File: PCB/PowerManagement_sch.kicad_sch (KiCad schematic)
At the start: 20 parts, among them CN1 S2B-PH-SM4-TB(LF)(SN), U1 BQ24074RGTR, U2 SGM2050XTRL20G/TR

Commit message: Finished schematic
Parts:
- C1: value 4.7uF 6.3V -> 4.7uF 10V
- C2: value 4.7uF -> 4.7uF 10V
- C3: value 1uF 6.3V -> 1uF 10V
- C4: value 10uF -> 10uF 10V
- C5: value 10uF -> 10uF 6.3V
- C6: value 100n -> 100nF 10V
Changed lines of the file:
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@@
 		(dnp no)
 		(property "Reference" "C5"
-			(at 243.078 66.802 90)
+			(at 243.078 71.882 90)
 			(effects
 				(font
@@
 			)
 		)
-		(property "Value" "10uF"
-			(at 235.204 67.056 90)
+		(property "Value" "10uF 6.3V"
+			(at 236.22 66.548 90)
 			(effects
 				(font
@@
 		(dnp no)
 		(property "Reference" "C6"
-			(at 258.064 101.6 90)
+			(at 252.73 101.6 90)
 			(effects
 				(font
@@
 			)
 		)
-		(property "Value" "100n"
-			(at 250.19 101.092 90)
+		(property "Value" "100nF 10V"
+			(at 250.952 106.172 90)
 			(effects
 				(font
@@
 			)
 		)
-		(property "Value" "1uF 6.3V"
+		(property "Value" "1uF 10V"
 			(at 112.268 153.924 0)
 			(effects
@@
 		(dnp no)
 		(property "Reference" "C4"
-			(at 258.064 96.52 90)
+			(at 252.222 96.52 90)
 			(effects
 				(font
@@
 			)
 		)
-		(property "Value" "10uF"
-			(at 250.19 96.012 90)
+		(property "Value" "10uF 10V"
+			(at 258.064 96.774 90)
 			(effects
 				(font
@@
 			)
 		)
-		(property "Value" "4.7uF 6.3V"
+		(property "Value" "4.7uF 10V"
 			(at 107.95 101.854 0)
 			(effects
@@
 			)
 		)
-		(property "Value" "4.7uF"
+		(property "Value" "4.7uF 10V"
 			(at 148.336 108.204 0)
 			(effects

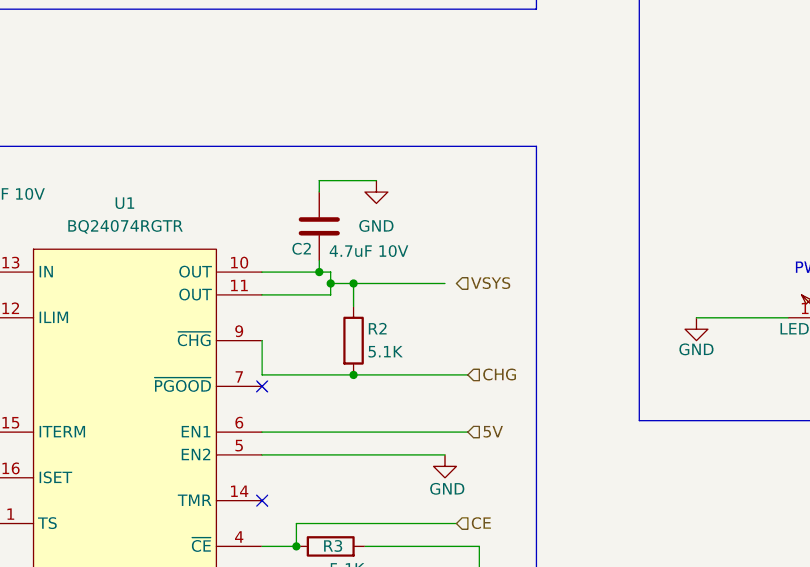
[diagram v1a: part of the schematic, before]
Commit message: pcb wired
- bldc driver + ldo left
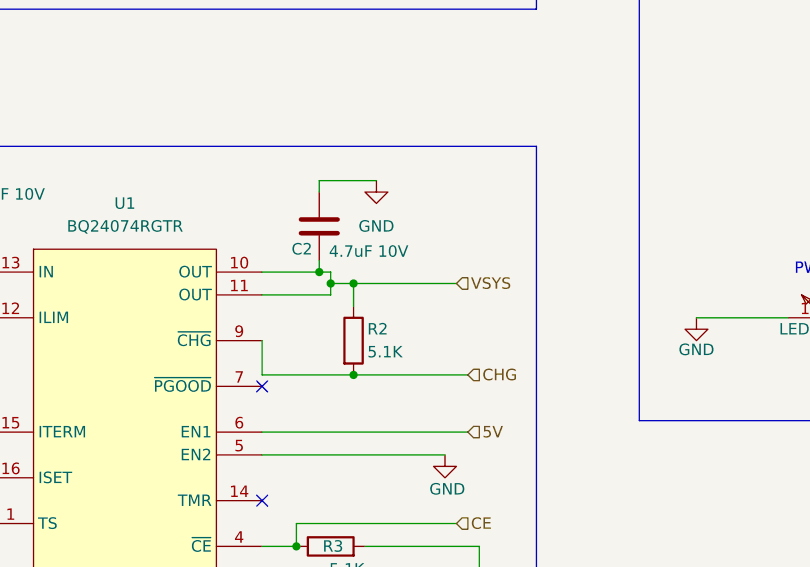
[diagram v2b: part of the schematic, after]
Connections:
- net VSYS: now also C2.1, R2.1, U1.10 (OUT), U1.11 (OUT)
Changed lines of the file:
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@@
 	(wire
 		(pts
-			(xy 142.24 111.76) (xy 152.4 111.76)
+			(xy 142.24 111.76) (xy 153.67 111.76)
 		)
 		(stroke

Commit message: PCB layout done
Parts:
- R1: value 2.2K -> 10K
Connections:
- no-connect marks 10 -> 13
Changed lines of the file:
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@@
 	)
 	(no_connect
+		(at 242.57 104.14)
+	)
+	(no_connect
 		(at 46.99 55.88)
 	)
@@
 	)
 	(no_connect
+		(at 217.17 91.44)
+	)
+	(no_connect
 		(at 46.99 40.64)
 	)
@@
 		(at 132.08 135.89)
 	)
+	(no_connect
+		(at 217.17 88.9)
+	)
 	(wire
 		(pts
@@
 			)
 		)
-		(property "Value" "2.2K"
+		(property "Value" "10K"
 			(at 208.28 115.57 90)
 			(effects

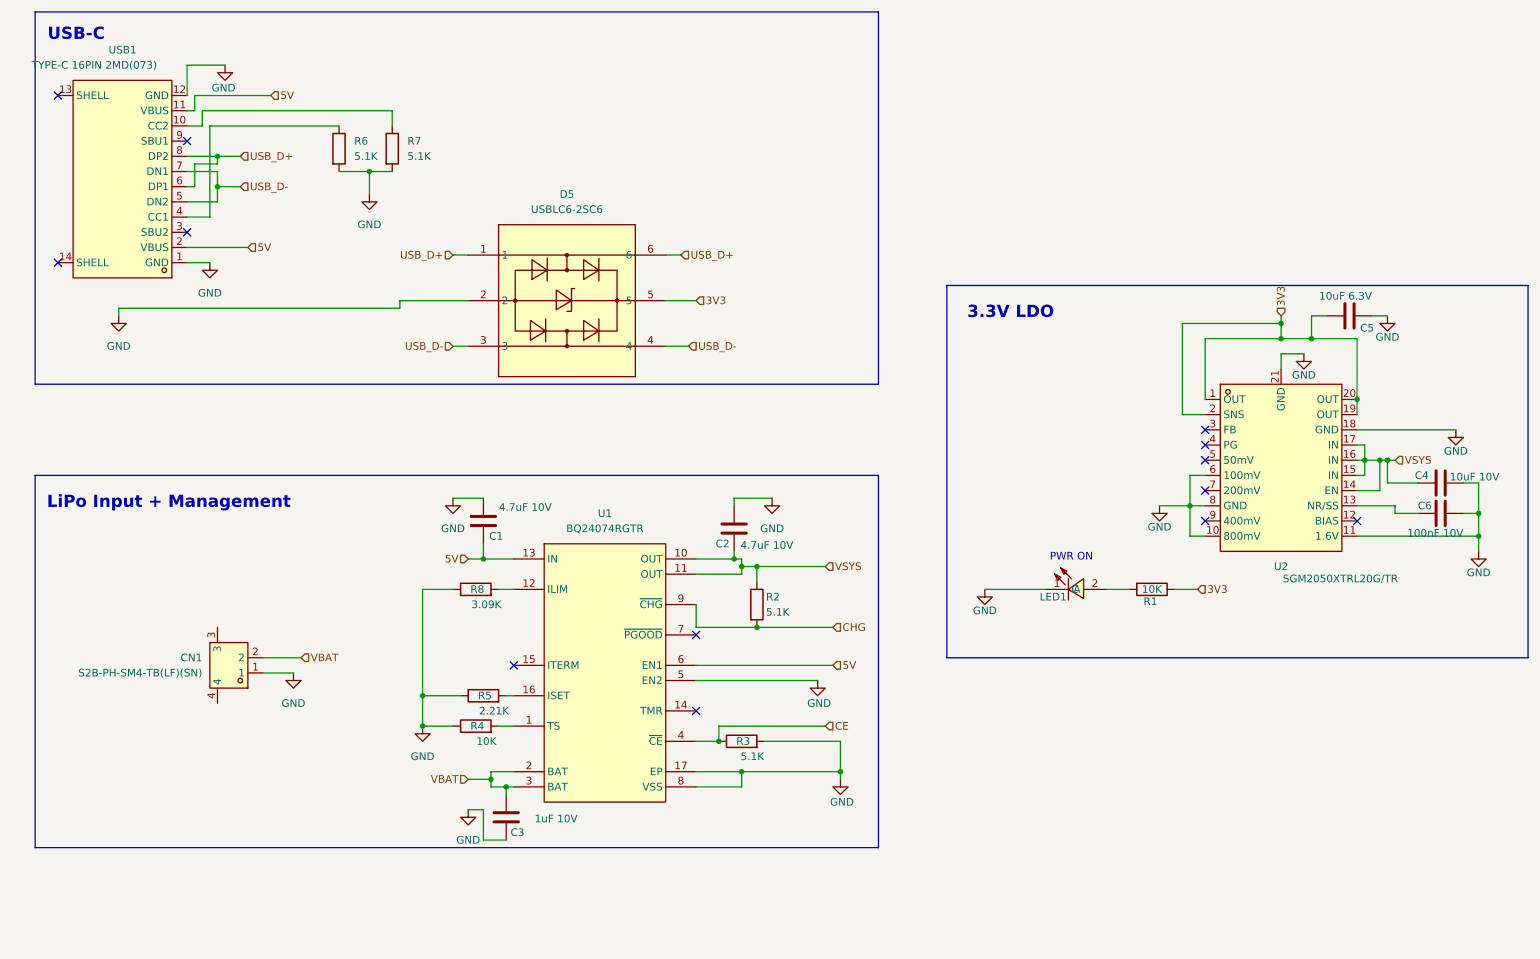
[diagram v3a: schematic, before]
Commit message: removed lipo circuitry
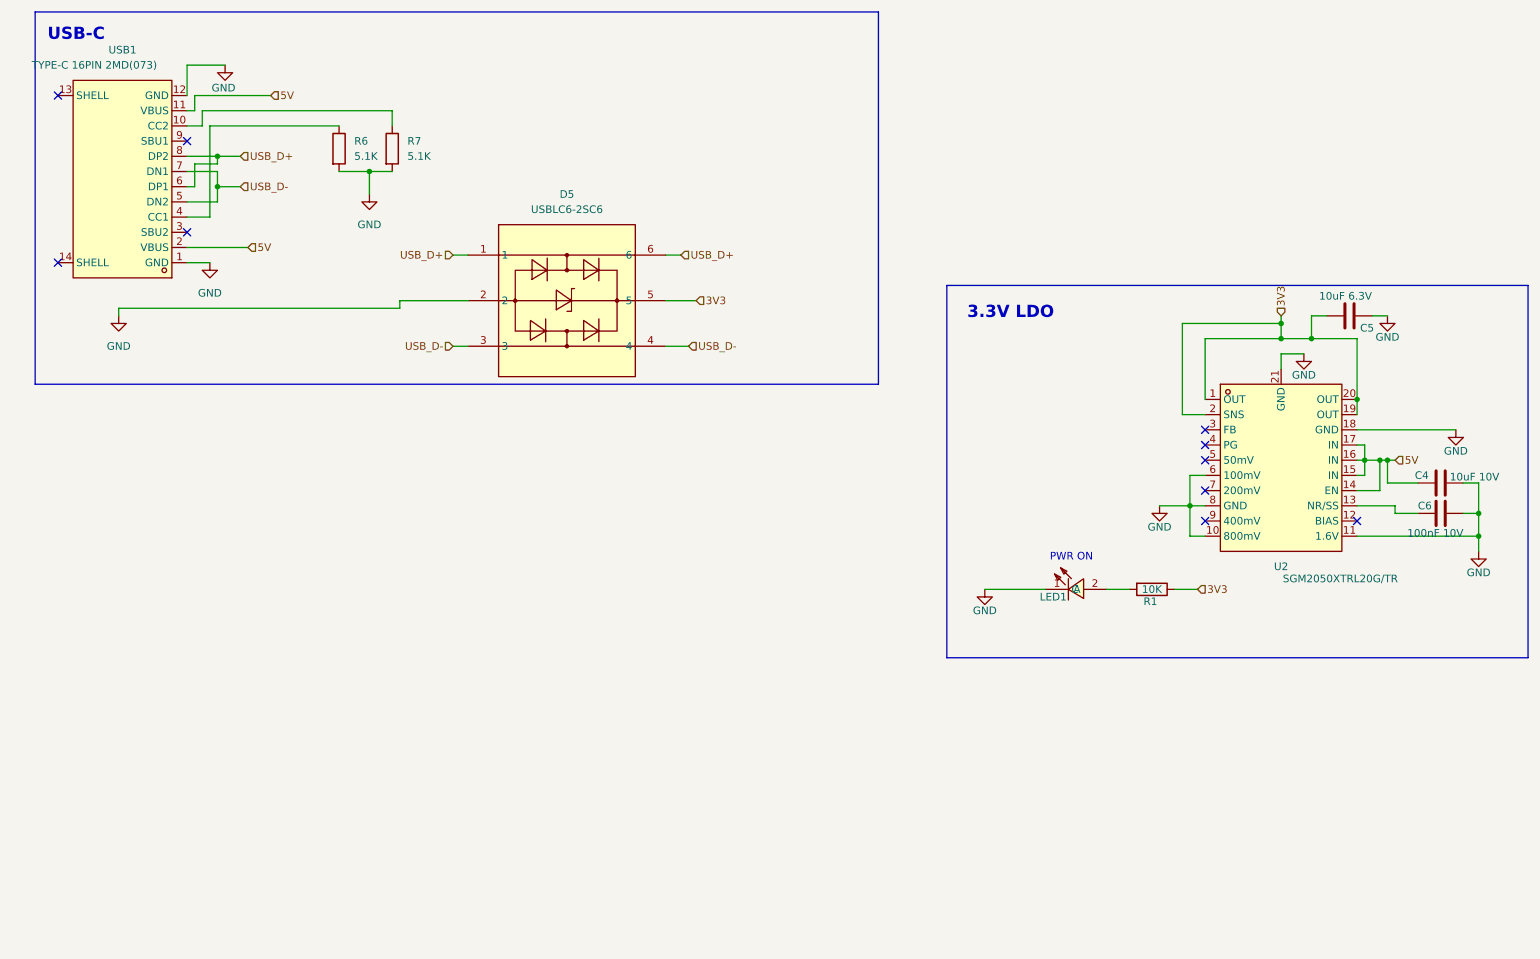
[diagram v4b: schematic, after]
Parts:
- removed C1, C2: 4.7uF 10V, Capacitor_SMD:C_0402_1005Metric, symbol Device:C
- removed C3: 1uF 10V, Capacitor_SMD:C_0402_1005Metric, symbol Device:C
- removed CN1: S2B-PH-SM4-TB(LF)(SN), easyeda2kicad:CONN-SMD_P2.00_S2B-PH-SM4-TB-LF-SN, symbol easyeda2kicad:S2B-PH-SM4-TB(LF)(SN)
- removed R2, R3: 5.1K, Resistor_SMD:R_0402_1005Metric_Pad0.72x0.64mm_HandSolder, symbol Device:R
- removed R4: 10K, Resistor_SMD:R_0402_1005Metric_Pad0.72x0.64mm_HandSolder, symbol Device:R
- removed R5: 2.21K, Resistor_SMD:R_0402_1005Metric_Pad0.72x0.64mm_HandSolder, symbol Device:R
- removed R8: 3.09K, Resistor_SMD:R_0402_1005Metric_Pad0.72x0.64mm_HandSolder, symbol Device:R
- removed U1: BQ24074RGTR, easyeda2kicad:QFN-16_L3.0-W3.0-P0.50-TL-EP1.7, symbol easyeda2kicad:BQ24074RGTR
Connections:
- net VSYS is gone; now on net 5V: C4.2, U2.14 (EN), U2.15 (IN), U2.16 (IN), U2.17 (IN)
- no-connect marks 13 -> 10
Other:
- note removed: "LiPo Input + Management"

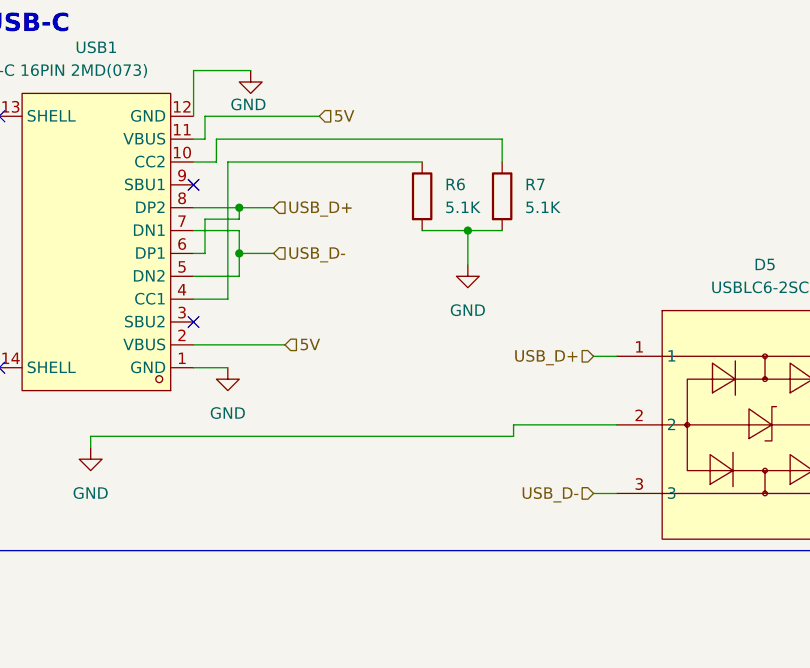
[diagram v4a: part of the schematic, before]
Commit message: PCB schematic checked - ready to trace
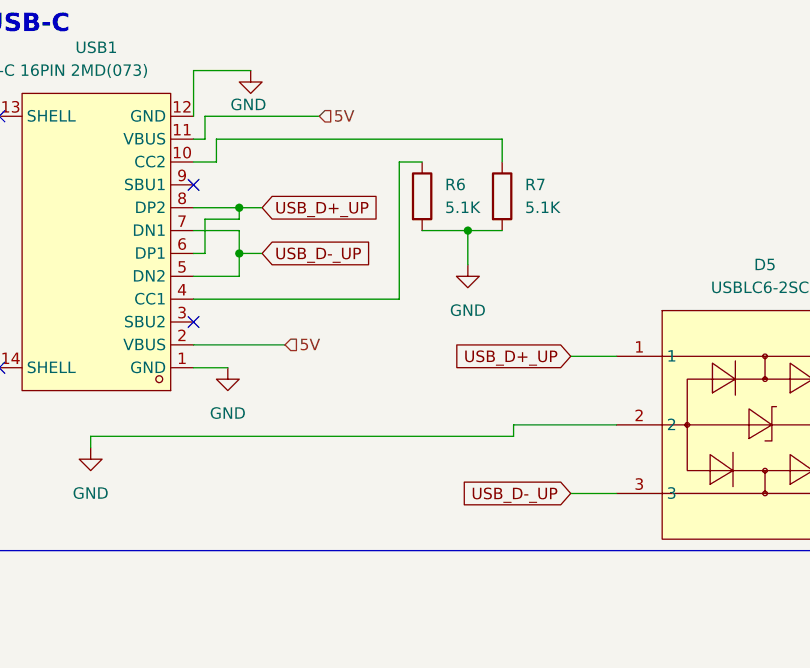
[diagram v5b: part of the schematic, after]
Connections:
- net USB_D+: no longer D5.1, USB1.6 (DP1), USB1.8 (DP2)
- net USB_D-: no longer D5.3, USB1.5 (DN2), USB1.7 (DN1)
- new net USB_D+_UP: D5.1, USB1.6 (DP1), USB1.8 (DP2)
- new net USB_D-_UP: D5.3, USB1.5 (DN2), USB1.7 (DN1)
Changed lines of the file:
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@@
+	)
+	(junction
+		(at 229.87 73.66)
+		(diameter 0)
+		(color 0 0 0 0)
+	)
+	(junction
+		(at 229.87 71.12)
+		(diameter 0)
+		(color 0 0 0 0)
+	)
+	(junction
+		(at 262.89 102.87)
+		(diameter 0)
+		(color 0 0 0 0)
+	)
+	(junction
+		(at 52.07 43.18)
+		(diameter 0)
+		(color 0 0 0 0)
+	)
+	(junction
+		(at 246.38 93.98)
+		(diameter 0)
+		(color 0 0 0 0)
+	)
+	(junction
+		(at 242.57 83.82)
+		(diameter 0)
+		(color 0 0 0 0)
 	)
 	(junction
 		(at 52.07 48.26)
-		(diameter 0)
-		(color 0 0 0 0)
-	)
-	(junction
-		(at 229.87 73.66)
-		(diameter 0)
-		(color 0 0 0 0)
-	)
-	(junction
-		(at 229.87 71.12)
-		(diameter 0)
-		(color 0 0 0 0)
-	)
-	(junction
-		(at 262.89 102.87)
-		(diameter 0)
-		(color 0 0 0 0)
-	)
-	(junction
-		(at 52.07 43.18)
-		(diameter 0)
-		(color 0 0 0 0)
-	)
-	(junction
-		(at 246.38 93.98)
-		(diameter 0)
-		(color 0 0 0 0)
-	)
-	(junction
-		(at 242.57 83.82)
 		(diameter 0)
 		(color 0 0 0 0)
@@
 	(wire
 		(pts
+			(xy 52.07 48.26) (xy 52.07 50.8)
+		)
+		(stroke
+			(width 0)
+			(type default)
+		)
+	)
+	(wire
+		(pts
 			(xy 242.57 99.06) (xy 246.38 99.06)
 		)
@@
 	(wire
 		(pts
-			(xy 52.07 48.26) (xy 52.07 50.8)
-		)
-		(stroke
-			(width 0)
-			(type default)
-		)
-	)
-	(wire
-		(pts
 			(xy 82.55 67.31) (xy 93.98 67.31)
 		)
@@
 	(wire
 		(pts
+			(xy 88.9 59.69) (xy 93.98 59.69)
+		)
+		(stroke
+			(width 0)
+			(type default)
+		)
+	)
+	(wire
+		(pts
 			(xy 46.99 27.94) (xy 53.34 27.94)
 		)
@@
 	(wire
 		(pts
-			(xy 52.07 48.26) (xy 55.88 48.26)
+			(xy 88.9 74.93) (xy 93.98 74.93)
 		)
 		(stroke
@@
 	(wire
 		(pts
-			(xy 91.44 59.69) (xy 93.98 59.69)
+			(xy 52.07 48.26) (xy 54.61 48.26)
 		)
 		(stroke
@@
 	(wire
 		(pts
-			(xy 50.8 53.34) (xy 50.8 38.1)
-		)
-		(stroke
-			(width 0)
-			(type default)
-		)
-	)
-	(wire
-		(pts
-			(xy 46.99 53.34) (xy 50.8 53.34)
-		)
-		(stroke
-			(width 0)
-			(type default)
-		)
-	)
-	(wire
-		(pts
-			(xy 52.07 43.18) (xy 55.88 43.18)
+			(xy 69.85 53.34) (xy 69.85 38.1)
+		)
+		(stroke
+			(width 0)
+			(type default)
+		)
+	)
+	(wire
+		(pts
+			(xy 46.99 53.34) (xy 69.85 53.34)
+		)
+		(stroke
+			(width 0)
+			(type default)
+		)
+	)
+	(wire
+		(pts
+			(xy 52.07 43.18) (xy 54.61 43.18)
 		)
 		(stroke
@@
 	(wire
 		(pts
-			(xy 91.44 74.93) (xy 93.98 74.93)
-		)
-		(stroke
-			(width 0)
-			(type default)
-		)
-	)
-	(wire
-		(pts
 			(xy 247.65 97.79) (xy 252.73 97.79)
 		)
@@
 	(wire
 		(pts
-			(xy 50.8 38.1) (xy 72.39 38.1)
+			(xy 69.85 38.1) (xy 72.39 38.1)
 		)
 		(stroke
@@
 		)
 	)
+	(global_label "USB_D-_UP"
+		(shape input)
+		(at 54.61 48.26 0)
+		(fields_autoplaced yes)
+		(effects
+			(font
+				(size 1.27 1.27)
+			)
+			(justify left)
+		)
+		(property "Intersheetrefs" "${INTERSHEET_REFS}"
+			(at 68.7833 48.26 0)
+			(effects
+				(font
+					(size 1.27 1.27)
+				)
+				(justify left)
+				(hide yes)
+			)
+		)
+	)
+	(global_label "USB_D+_UP"
+		(shape input)
+		(at 88.9 59.69 180)
+		(fields_autoplaced yes)
+		(effects
+			(font
+				(size 1.27 1.27)
+			)
+			(justify right)
+		)
+		(property "Intersheetrefs" "${INTERSHEET_REFS}"
+			(at 74.7267 59.69 0)
+			(effects
+				(font
+					(size 1.27 1.27)
+				)
+				(justify right)
+				(hide yes)
+			)
+		)
+	)
+	(global_label "USB_D-_UP"
+		(shape input)
+		(at 88.9 74.93 180)
+		(fields_autoplaced yes)
+		(effects
+			(font
+				(size 1.27 1.27)
+			)
+			(justify right)
+		)
+		(property "Intersheetrefs" "${INTERSHEET_REFS}"
+			(at 74.7267 74.93 0)
+			(effects
+				(font
+					(size 1.27 1.27)
+				)
+				(justify right)
+				(hide yes)
+			)
+		)
+	)
+	(global_label "USB_D+_UP"
+		(shape input)
+		(at 54.61 43.18 0)
+		(fields_autoplaced yes)
+		(effects
+			(font
+				(size 1.27 1.27)
+			)
+			(justify left)
+		)
+		(property "Intersheetrefs" "${INTERSHEET_REFS}"
+			(at 68.7833 43.18 0)
+			(effects
+				(font
+					(size 1.27 1.27)
+				)
+				(justify left)
+				(hide yes)
+			)
+		)
+	)
 	(hierarchical_label "USB_D+"
 		(shape input)
@@
 		)
 	)
-	(hierarchical_label "USB_D+"
-		(shape input)
-		(at 91.44 59.69 180)
+	(hierarchical_label "5V"
+		(shape input)
+		(at 57.15 58.42 0)
 		(effects
 			(font
 				(size 1.27 1.27)
 			)
-			(justify right)
+			(justify left)
+		)
+	)
+	(hierarchical_label "3V3"
+		(shape input)
+		(at 132.08 67.31 0)
+		(effects
+			(font
+				(size 1.27 1.27)
+			)
+			(justify left)
+		)
+	)
+	(hierarchical_label "USB_D-"
+		(shape input)
+		(at 130.81 74.93 0)
+		(effects
+			(font
+				(size 1.27 1.27)
+			)
+			(justify left)
 		)
 	)
 	(hierarchical_label "5V"
 		(shape input)
-		(at 57.15 58.42 0)
+		(at 60.96 33.02 0)
 		(effects
 			(font
@@
 	(hierarchical_label "3V3"
 		(shape input)
-		(at 132.08 67.31 0)
+		(at 229.87 69.85 90)
 		(effects
 			(font
@@
 		)
 	)
-	(hierarchical_label "USB_D+"
-		(shape input)
-		(at 55.88 43.18 0)
-		(effects
-			(font
-				(size 1.27 1.27)
-			)
-			(justify left)
-		)
-	)
-	(hierarchical_label "USB_D-"
-		(shape input)
-		(at 91.44 74.93 180)
-		(effects
-			(font
-				(size 1.27 1.27)
-			)
-			(justify right)
-		)
-	)
-	(hierarchical_label "USB_D-"
-		(shape input)
-		(at 130.81 74.93 0)
-		(effects
-			(font
-				(size 1.27 1.27)
-			)
-			(justify left)
-		)
-	)
-	(hierarchical_label "5V"
-		(shape input)
-		(at 60.96 33.02 0)
-		(effects
-			(font
-				(size 1.27 1.27)
-			)
-			(justify left)
-		)
-	)
 	(hierarchical_label "3V3"
 		(shape input)
-		(at 229.87 69.85 90)
-		(effects
-			(font
-				(size 1.27 1.27)
-			)
-			(justify left)
-		)
-	)
-	(hierarchical_label "3V3"
-		(shape input)
 		(at 215.9 115.57 0)
 		(effects
 			(font
-				(size 1.27 1.27)
-			)
-			(justify left)
-		)
-	)
-	(hierarchical_label "USB_D-"
-		(shape input)
-		(at 55.88 48.26 0)
-		(effects
-			(font
